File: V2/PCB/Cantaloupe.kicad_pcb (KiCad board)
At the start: 2 copper layers, 143.9 x 118.7 mm, 124 parts, among them J1 USB_In, J2 OLED, J3 Link, J4 Debug, J5 Trackball, Q1 2N7002, Q2 AO3401A, SW1 MX, SW10 MX, SW11 MX, SW12 MX, SW13 MX, SW14 MX, SW15 MX, SW16 MX, SW17 MX, SW18 MX, SW19 MX, SW2 MX, SW20 MX, SW21 MX, SW22 MX, SW23 MX, SW24 MX, SW25 MX, SW26 MX, SW27 MX, SW28 MX, SW29 MX, SW3 MX, SW30 MX, SW31 Encoder, SW32 MX, SW4 MX, SW5 MX, SW6 MX, SW7 MX, SW8 MX, SW9 MX, U1 STM32F4x1CxUx, U2 SRV05-4, U3 SRV05-4, U4 XC6206P332MR, U5 LMV321, Y1 8MHz

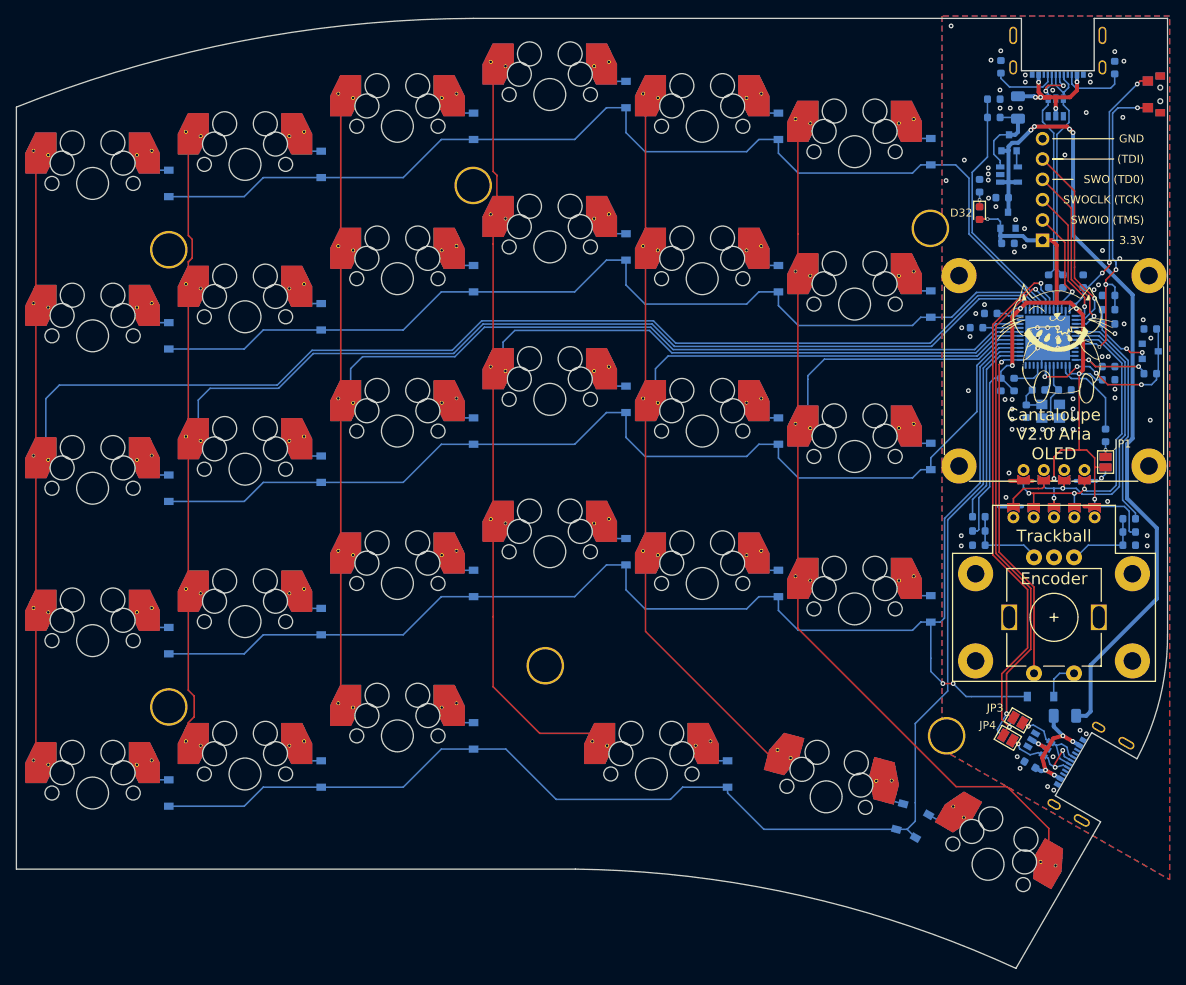
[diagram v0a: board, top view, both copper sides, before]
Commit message: New plate files, removed internal holes from PCB
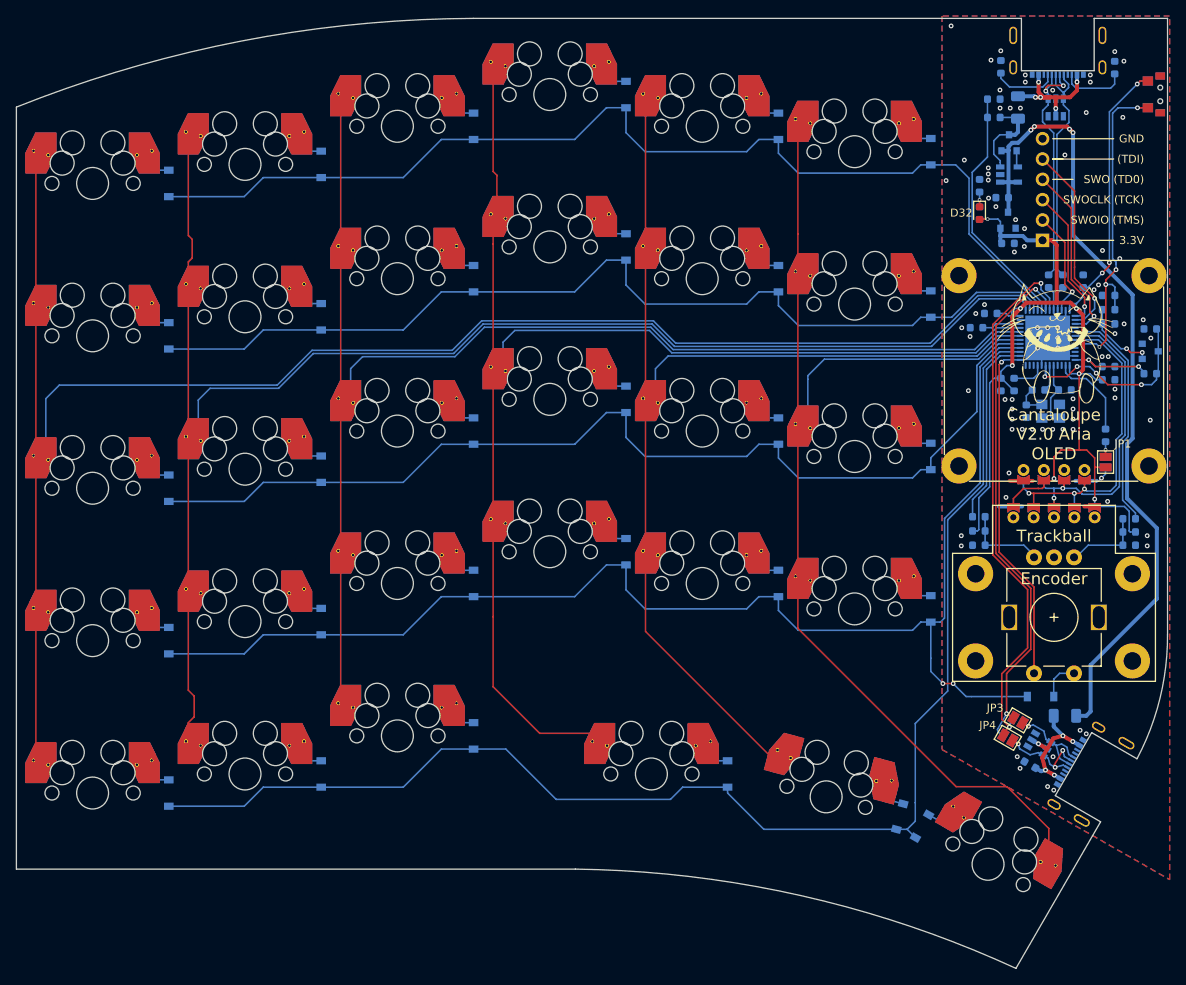
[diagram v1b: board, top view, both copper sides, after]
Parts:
- removed H1, H2, H3, H4, H5, H6: Hole, Ariamelon:HOLE_M2_TH
